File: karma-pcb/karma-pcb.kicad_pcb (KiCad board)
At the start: 2 copper layers, 255.5 x 103.3 mm, 86 parts, among them J1 BAT, J2 BAT, U1 xiao-ble, U2 xiao-ble

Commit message: Update PCB layout to rev 0.2
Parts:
- moved DR16 19.1 mm to (161.9, 119.7), turned to -60 degrees
- moved DL1 18.6 mm to (35.8, 55.5), turned to -90 degrees
- moved DL10 18.6 mm to (109.8, 64.8), turned to -90 degrees
- moved DL11 18.6 mm to (35.8, 92.5), turned to -90 degrees
- moved DL12 18.6 mm to (54.3, 78.6), turned to -90 degrees
- moved DL13 18.6 mm to (72.8, 71.7), turned to -90 degrees
- moved DL15 18.6 mm to (109.8, 83.2), turned to -90 degrees
- moved DL18 18.6 mm to (135.3, 111.6), turned to -120 degrees
- moved DL2 18.6 mm to (54.3, 41.6), turned to -90 degrees
- moved DL3 18.6 mm to (72.8, 34.7), turned to -90 degrees
- moved DL4 18.6 mm to (91.3, 41.6), turned to -90 degrees
- moved DL5 18.6 mm to (109.8, 46.2), turned to -90 degrees
- moved DL6 18.6 mm to (35.8, 74.0), turned to -90 degrees
- moved DL7 18.6 mm to (54.3, 60.1), turned to -90 degrees
- moved DL8 18.6 mm to (72.8, 53.2), turned to -90 degrees
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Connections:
- U1 pad 1: ROW0_L -> ROW3_L
- U1 pad 2: ROW1_L -> ROW2_L
- U1 pad 3: ROW2_L -> ROW1_L
- U1 pad 4: ROW3_L -> ROW0_L
- U2 pad 1: ROW0_R -> unconnected-(U2-A2/0.02_H-Pad1)
- U2 pad 10: COL3_R -> ROW2_R
- U2 pad 11: COL2_R -> ROW3_R
- U2 pad 2: ROW1_R -> unconnected-(U2-A4/0.03_H-Pad2)
- U2 pad 3: ROW2_R -> COL0_R
- U2 pad 4: ROW3_R -> COL1_R
- U2 pad 5: COL0_R -> COL2_R
- U2 pad 6: COL1_R -> COL3_R
- U2 pad 7: unconnected-(U2-B8_TX/1.11-Pad7) -> COL4_R
- U2 pad 8: unconnected-(U2-B9_RX/1.12-Pad8) -> ROW0_R
- U2 pad 9: COL4_R -> ROW1_R
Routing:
- net COL2_R: track 183.9 -> 120.2 mm, vias 5 -> 0
- net COL3_R: track 211.6 -> 154.6 mm, vias 5 -> 0
- net COL4_R: track 228.8 -> 178.7 mm
- net ROW2_L: track 182.4 -> 139.7 mm, vias 0 -> 8
- net ROW0_L: track 135.6 -> 94.1 mm, vias 0 -> 4
- net COL1_R: track 114.5 -> 73.3 mm, vias 4 -> 0
- net ROW1_L: track 161.4 -> 120.9 mm, vias 0 -> 8
- net ROW3_L: track 196.5 -> 161.9 mm, vias 0 -> 2
- net ROW0_R: track 133.7 -> 99.7 mm, vias 2 -> 8
- net COL1_L: track 96.2 -> 63.6 mm, vias 2 -> 0
- net ROW1_R: track 151.6 -> 119.6 mm, vias 2 -> 8
- net ROW2_R: track 169.8 -> 139.2 mm, vias 2 -> 8
- net COL2_L: track 173.8 -> 143.8 mm, vias 3 -> 0
- net COL0_R: track 100.5 -> 72.6 mm, vias 4 -> 0
- net COL3_L: track 190.8 -> 164.2 mm, vias 3 -> 0
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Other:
- board text removed: "BATTERY"

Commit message: Add via stitching
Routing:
- net COL4_L: track 188.8 -> 194.3 mm
- net ROW0_R: track 99.7 -> 101.7 mm
- net GND_R: vias 0 -> 44
- net GND_L: vias 0 -> 48
- added copper zone on B.Cu, net GND_L
- added copper zone on B.Cu, net GND_R

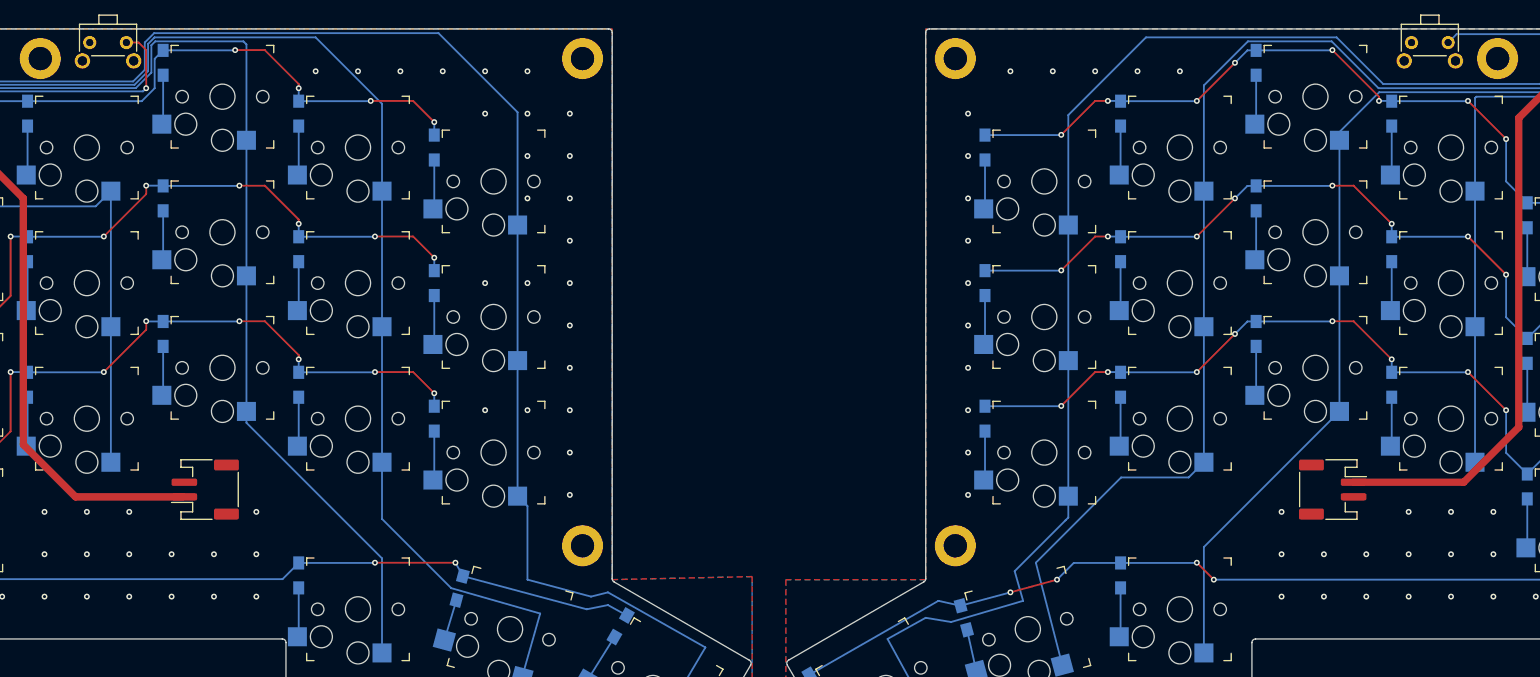
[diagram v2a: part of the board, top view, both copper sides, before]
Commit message: Add silkscreen labels
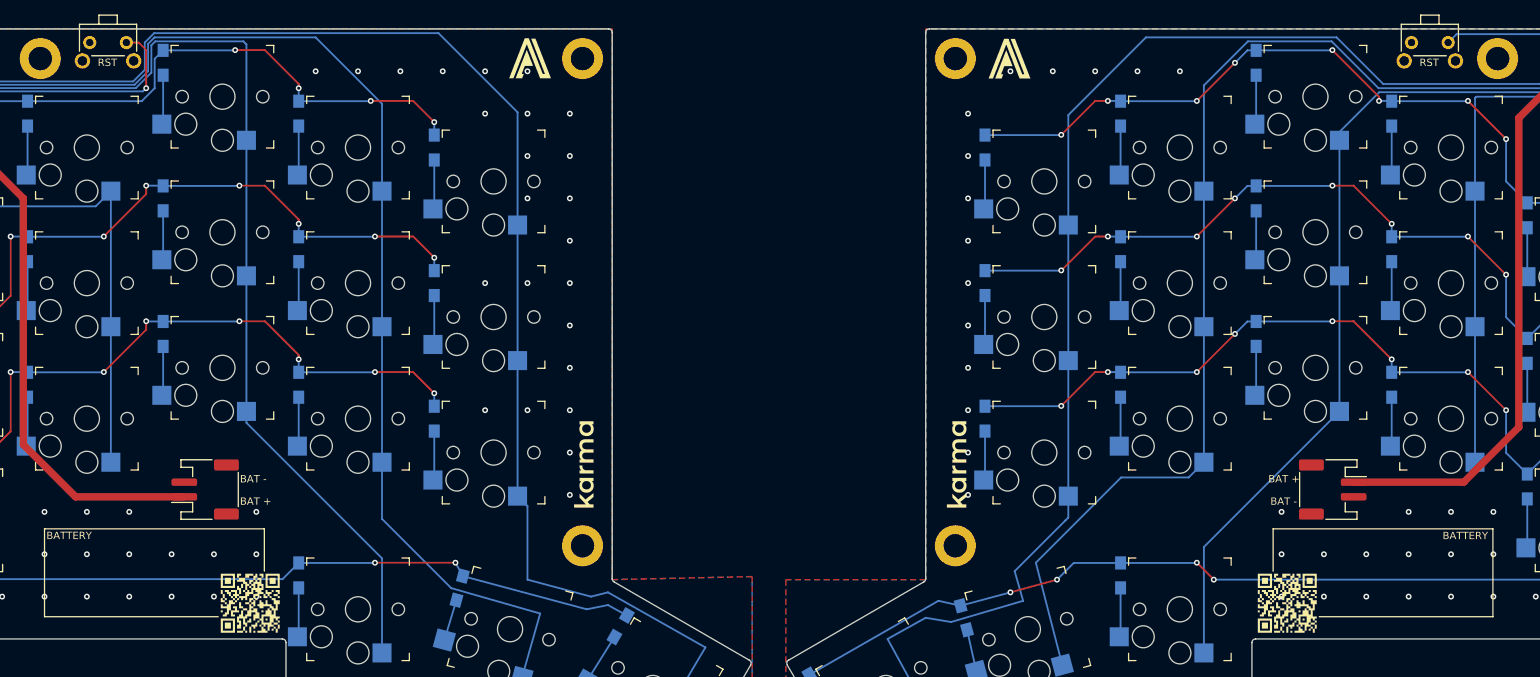
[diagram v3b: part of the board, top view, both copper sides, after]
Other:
- board text added: "BAT +"
- board text added: "BAT -"
- board text added: "BATTERY"
- board text added: "RST"

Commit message: Add silkscreen label for controller
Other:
- board text added: "XIAO nRF52840"

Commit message: Add 3D model for keycaps
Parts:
- J1, J2: footprint Connector_JST:JST_PH_S2B-PH-SM4-TB_1x02-1MP_P2.00mm_Horizontal -> karmalib:JST_PH_S2B-PH-SM4-TB

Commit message: Update left PCB layout to rev 0.3
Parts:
- removed the REF** at (279.2, 109.3)
- removed the REF** at (31.8, 109.3)
- removed the REF** at (181.0, 34.1)
- removed the REF** at (130.1, 100.6)
- removed the REF** at (255.0, 34.1)
- removed the REF** at (181.0, 100.6)
- removed the REF** at (130.1, 34.1)
- removed the REF** at (56.1, 34.1)
- added REF**: MountingHole_2.2mm_M2_DIN965_Pad, MountingHole:MountingHole_2.2mm_M2_DIN965_Pad, F.Cu at (131.8, 103.1)
- added REF**: MountingHole_2.2mm_M2_DIN965_Pad, MountingHole:MountingHole_2.2mm_M2_DIN965_Pad, F.Cu at (31.7, 113.5)
- added REF**: MountingHole_2.2mm_M2_DIN965_Pad, MountingHole:MountingHole_2.2mm_M2_DIN965_Pad, F.Cu at (131.8, 35.8)
- added REF**: MountingHole_2.2mm_M2_DIN965_Pad, MountingHole:MountingHole_2.2mm_M2_DIN965_Pad, F.Cu at (55.4, 35.8)
- moved RSW1 50.5 mm to (115.7, 37.0)
- moved SWL11 4.53 mm to (43.9, 101.7)
- moved SWL6 4.03 mm to (43.9, 82.7)
- moved U1 3.65 mm to (40.1, 43.7)
- moved SWL13 3.63 mm to (81.9, 79.8)
- moved SWL1 3.52 mm to (43.9, 63.6)
- moved SWL15 3.48 mm to (119.9, 90.7)
- moved SWL8 3.15 mm to (81.9, 60.8)
- moved SWL14 3.11 mm to (100.9, 86.0)
- moved SWL10 3.09 mm to (119.9, 71.7)
- moved J1 3.03 mm to (78.6, 96.0)
- moved DL11 2.97 mm to (35.8, 95.5)
- moved SWL12 2.77 mm to (62.9, 86.0)
- moved SWL5 2.72 mm to (119.9, 52.7)
- moved SWL9 2.68 mm to (100.9, 67.0)
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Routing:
- net COL4_L: track 194.3 -> 0.00 mm
- net COL4_R: track 178.7 -> 0.21 mm
- net ROW3_R: track 174.2 -> 0.15 mm, vias 4 -> 0
- net COL3_L: track 164.2 -> 0.00 mm
- net ROW3_L: track 161.9 -> 0.00 mm, vias 2 -> 0
- net COL3_R: track 154.6 -> 0.00 mm
- net COL2_L: track 143.8 -> 0.00 mm
- net ROW2_L: track 139.7 -> 0.00 mm, vias 8 -> 0
- net ROW2_R: track 139.2 -> 0.05 mm, vias 8 -> 0
- net ROW1_L: track 120.9 -> 0.00 mm, vias 8 -> 0
- net ROW1_R: track 119.6 -> 0.05 mm, vias 8 -> 0
- net COL2_R: track 120.2 -> 1.13 mm
- net ROW0_R: track 101.7 -> 0.13 mm, vias 8 -> 0
- net ROW0_L: track 94.1 -> 0.00 mm, vias 4 -> 0
- net VBAT_R: track 85.7 -> 0.00 mm
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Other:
- board size 255.5 x 103.3 mm -> 253.8 x 105.6 mm
